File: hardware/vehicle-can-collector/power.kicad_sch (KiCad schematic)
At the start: 42 parts, among them Q501 MMBT3906, Q502 DMG2301L, Q503 2N7002, Q504 2N7002, Q505 DMG2301L, Q506 DMG2301L, Q507 DMG2301L, U501 LMZ12001TZX-ADJ_NOPB, U502 LP38693MP-3.3, U503 LM317L_SOT-89

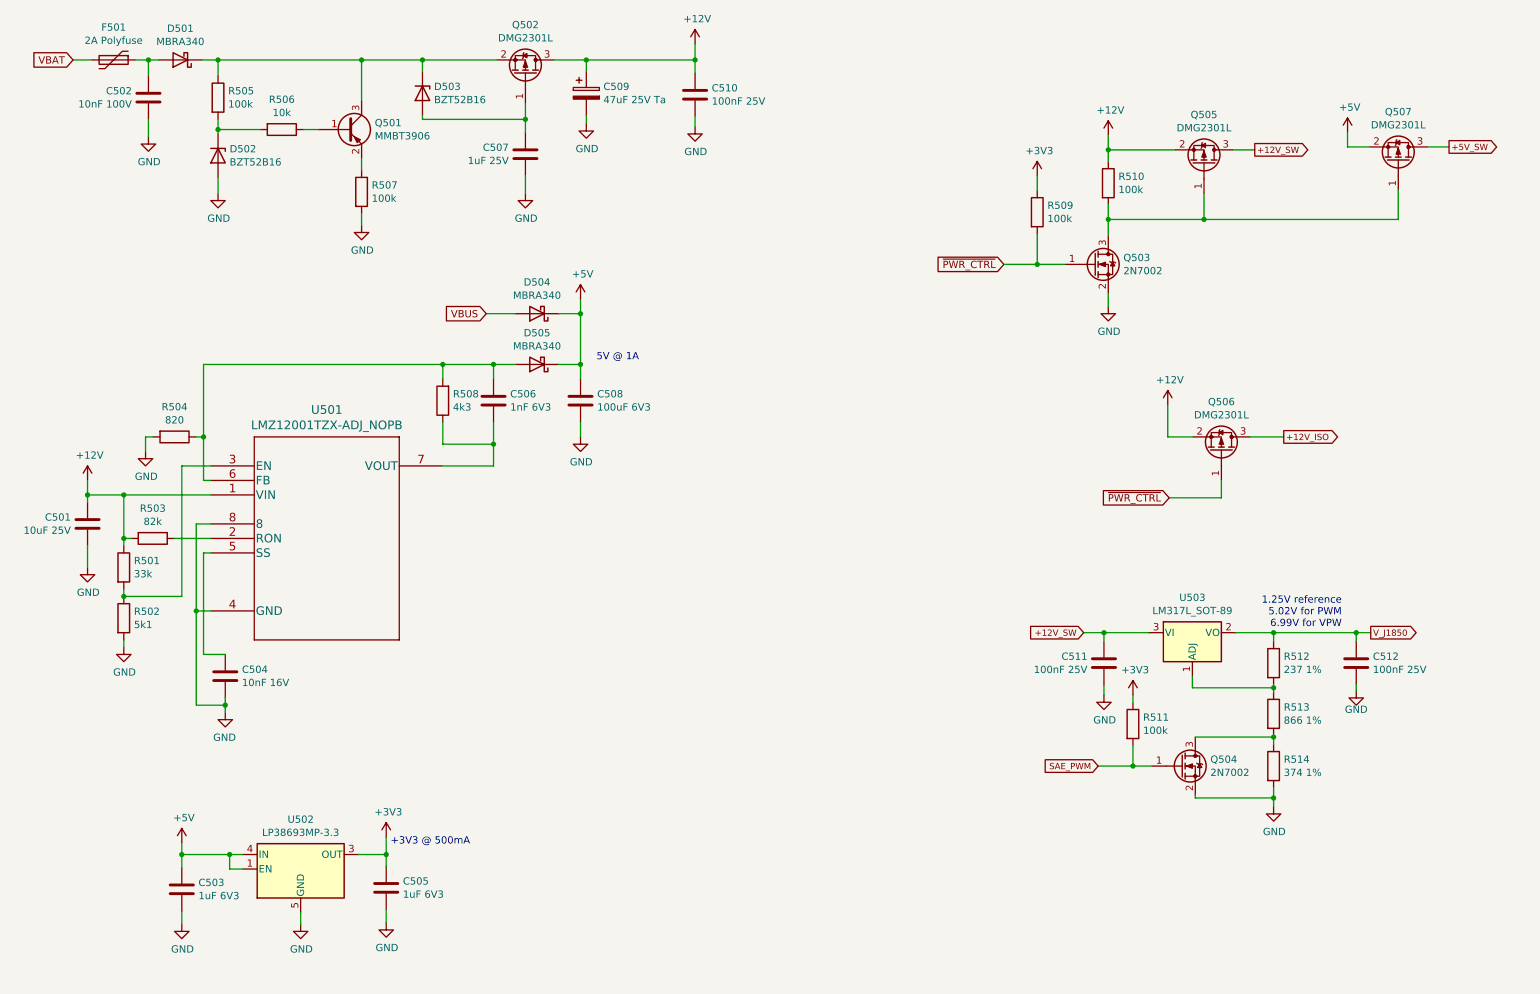
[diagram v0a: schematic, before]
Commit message: Added decoupling, more LEDs, update dts
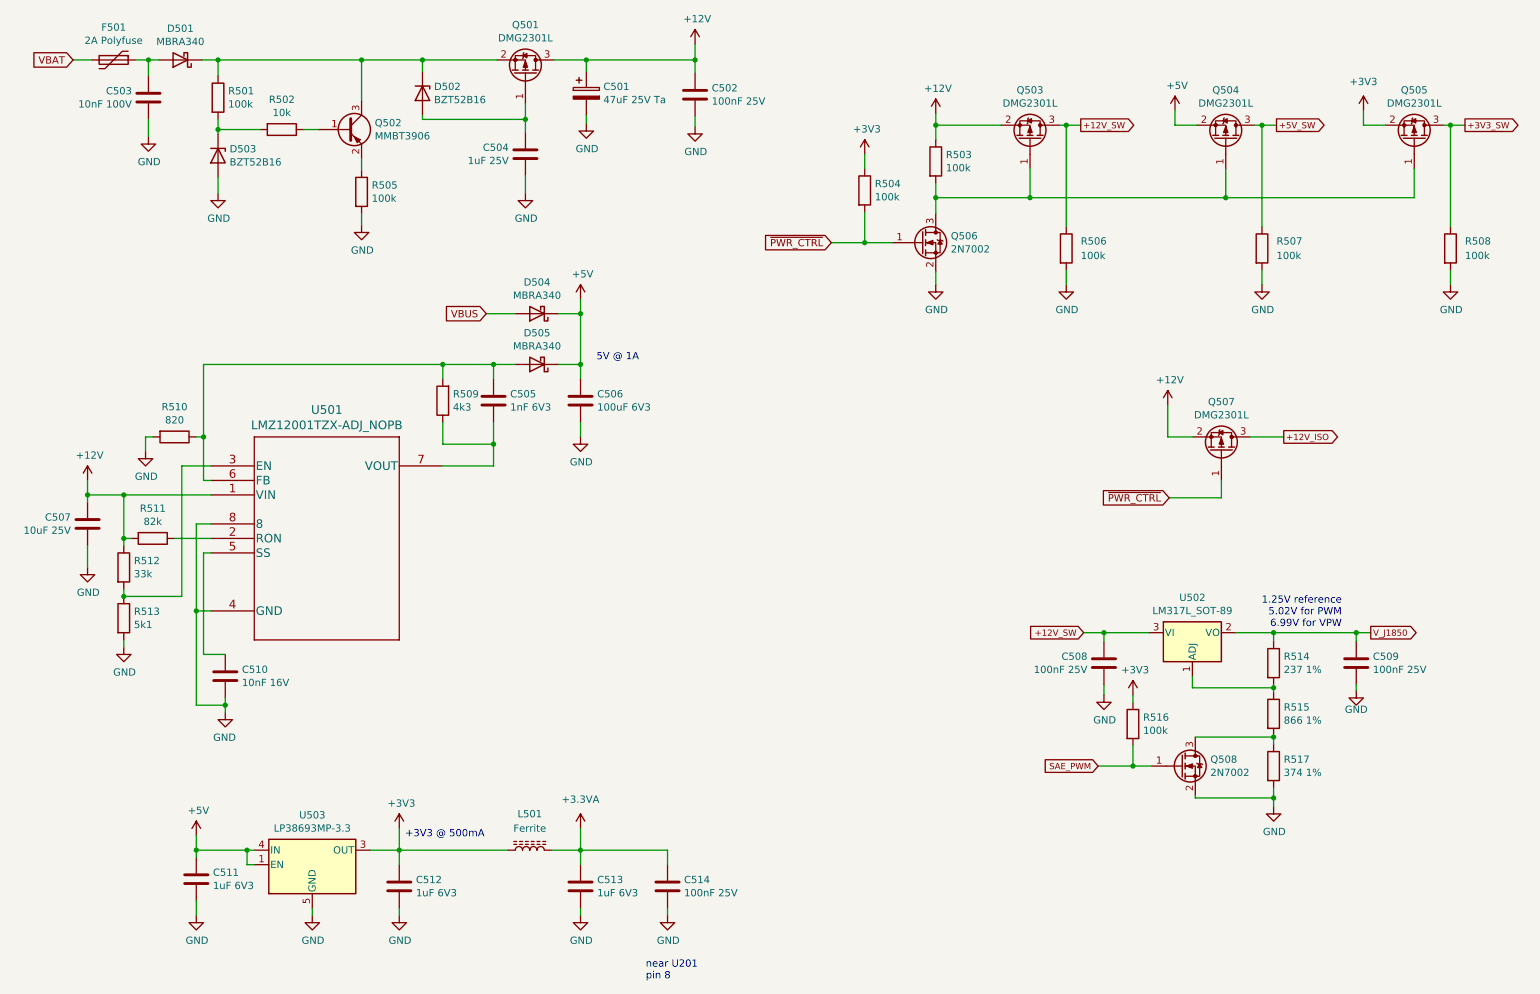
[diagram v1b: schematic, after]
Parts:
- added C513: 1uF 6V3, symbol Device:C
- added C514: 100nF 25V, symbol Device:C
- added L501: Ferrite, Inductor_SMD:L_0805_2012Metric_Pad1.05x1.20mm_HandSolder, symbol Device:L_Ferrite
- added Q505: DMG2301L, Package_TO_SOT_SMD:SOT-23, symbol Transistor_FET:DMG2301L
- added R506, R507, R508: 100k, symbol Device:R
- renumbered C509 to C501, C510 to C502, C502 to C503, C507 to C504, C506 to C505, C508 to C506, C501 to C507, C511 to C508, C512 to C509, C504 to C510, C503 to C511, C505 to C512, D503 to D502, D502 to D503, Q502 to Q501, Q501 to Q502, Q505 to Q503, Q507 to Q504, Q503 to Q506, Q506 to Q507, Q504 to Q508, R505 to R501, R506 to R502, R510 to R503, R509 to R504, R507 to R505, R508 to R509, R504 to R510, R503 to R511, R501 to R512, R502 to R513, R512 to R514, R513 to R515, R511 to R516, R514 to R517, U503 to U502, U502 to U503
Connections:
- net +12V_SW: now also R506.1
- net +3V3: now also L501.1, Q505.2 (S)
- net +5V_SW: now also R507.1
- net GND: now also C513.2, C514.1, R506.2, R507.2, R508.2
- net at Q503.1 (G), Q504.1 (G), Q506.3 (D)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: now also Q505.1 (G)
- new net +3.3VA: C513.1, C514.2, L501.2
- new net +3V3_SW: Q505.3 (D), R508.1
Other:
- note added: "near U201 pin 8"
- company: (none) -> Gavin Hurlbut
- title: (none) -> Vehicle CAN Collector
- moved on the sheet: C511, C512, Q503, Q504, Q506, R503, R504, U503

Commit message: Added footprints, tossed all footprints onto PCB
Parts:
- C501: footprint (none) -> Capacitor_Tantalum_SMD:CP_EIA-7343-31_Kemet-D_Pad2.25x2.55mm_HandSolder
- C502, C503, C504, C505, C506, C507, C508, C509, C510, C511, C512, C513, C514: footprint (none) -> Capacitor_SMD:C_0805_2012Metric_Pad1.18x1.45mm_HandSolder
- F501, R501, R502, R503, R504, R505, R506, R507, R508, R509, R510, R511, R512, R513, R514, R515, R516, R517: footprint (none) -> Resistor_SMD:R_0805_2012Metric_Pad1.20x1.40mm_HandSolder
- U501: footprint TZA07A -> UltraLibrarian:LMZ12001TZX-ADJ&slash_NOPB
